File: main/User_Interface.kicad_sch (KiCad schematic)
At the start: 0 parts

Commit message: added UI, +12/gnd to 4 pin adapter symbol, added NMEA2000 gateway symbol
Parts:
- added UI: ~, symbol New_Library_0:Monitor
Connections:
- new net 4_pin_power: UI. (Radar_port_Ethernet)
- new net 9_pin_sonar: UI. (Radar_port_Ethernet)
- new net NMEA2000: UI. (Radar_port_Ethernet)
- new net Radar_port_ethernet: UI. (Radar_port_Ethernet)
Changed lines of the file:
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@@
 	(generator_version "8.0")
 	(paper "A4")
+	(hierarchical_label "Radar_port_ethernet"
+		(shape input)
+		(at 133.35 114.3 270)
+		(fields_autoplaced yes)
+		(effects
+			(font
+				(size 1.27 1.27)
+			)
+			(justify right)
+		)
+	)
+	(hierarchical_label "NMEA2000"
+		(shape input)
+		(at 138.43 114.3 270)
+		(fields_autoplaced yes)
+		(effects
+			(font
+				(size 1.27 1.27)
+			)
+			(justify right)
+		)
+	)
+	(hierarchical_label "4_pin_power"
+		(shape input)
+		(at 163.83 114.3 270)
+		(fields_autoplaced yes)
+		(effects
+			(font
+				(size 1.27 1.27)
+			)
+			(justify right)
+		)
+	)
+	(hierarchical_label "9_pin_sonar"
+		(shape input)
+		(at 168.91 114.3 270)
+		(fields_autoplaced yes)
+		(effects
+			(font
+				(size 1.27 1.27)
+			)
+			(justify right)
+		)
+	)
+	(symbol
+		(lib_id "New_Library_0:Monitor")
+		(at 151.13 99.06 0)
+		(unit 1)
+		(exclude_from_sim no)
+		(in_bom yes)
+		(on_board yes)
+		(dnp no)
+		(property "Reference" "UI"
+			(at 149.352 72.136 0)
+			(effects
+				(font
+					(size 1.27 1.27)
+				)
+				(justify left)
+			)
+		)
+		(property "Value" "~"
+			(at 177.8 93.98 0)
+			(effects
+				(font
+					(size 1.27 1.27)
+				)
+				(justify left)
+			)
+		)
+		(property "Footprint" ""
+			(at 151.13 99.06 0)
+			(effects
+				(font
+					(size 1.27 1.27)
+				)
+				(hide yes)
+			)
+		)
+		(property "Datasheet" ""
+			(at 151.13 99.06 0)
+			(effects
+				(font
+					(size 1.27 1.27)
+				)
+				(hide yes)
+			)
+		)
+		(property "Description" ""
+			(at 151.13 99.06 0)
+			(effects
+				(font
+					(size 1.27 1.27)
+				)
+				(hide yes)
+			)
+		)
+		(pin ""
+		)
+		(pin ""
+		)
+		(pin ""
+		)
+		(pin ""
+		)
+		(instances
+			(project ""
+				(path "/54fbbba9-a737-4199-9a4b-f9fa49b3de5e/3ec4e0ef-19c3-4e21-bb09-251ed42858ce"
+					(reference "UI")
+					(unit 1)
+				)
+			)
+		)
+	)
 )

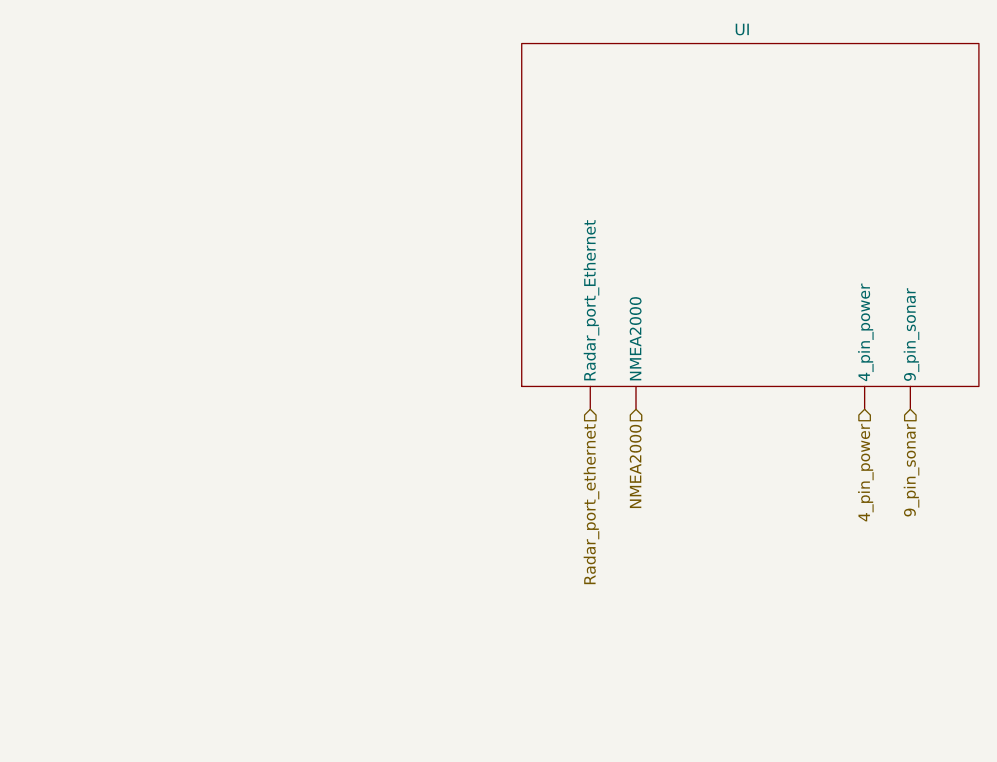
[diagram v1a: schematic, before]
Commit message: Added AMS, LEDs
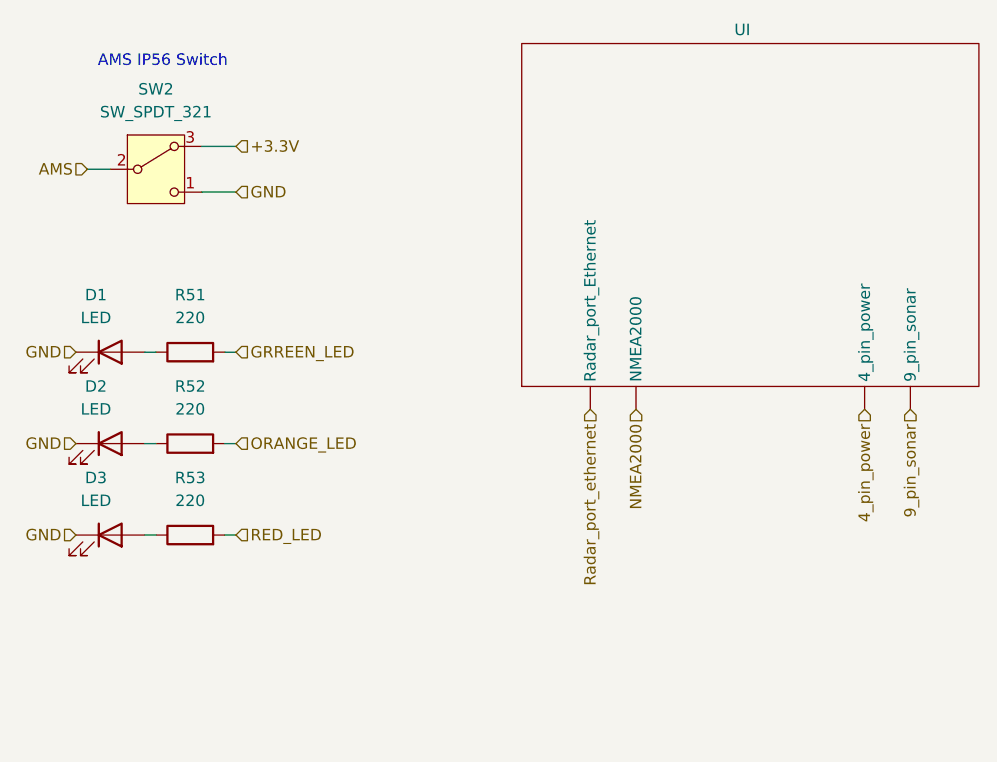
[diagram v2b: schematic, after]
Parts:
- added D1, D2, D3: LED, symbol Device:LED
- added R51, R52, R53: 220, symbol Device:R
- added SW2: SW_SPDT_321, symbol Switch:SW_SPDT_321
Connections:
- new net: D1.2 (A), R51.1
- new net: D3.2 (A), R53.1
- new net: D2.2 (A), R52.1
- new net +3.3V: SW2.3 (A)
- new net AMS: SW2.2 (B)
- new net GND: D1.1 (K), D2.1 (K), D3.1 (K), SW2.1 (C)
- new net GRREEN_LED: R51.2
- new net ORANGE_LED: R52.2
- new net RED_LED: R53.2
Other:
- note added: "AMS IP56 Switch"

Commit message: added logos, oranised sheets, final version
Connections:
- net Radar_port_ethernet renamed Radar
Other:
- company: (none) -> Designers: Krzysztof Grajek, Wojtek Kołodziej
- title: (none) -> UI schematic

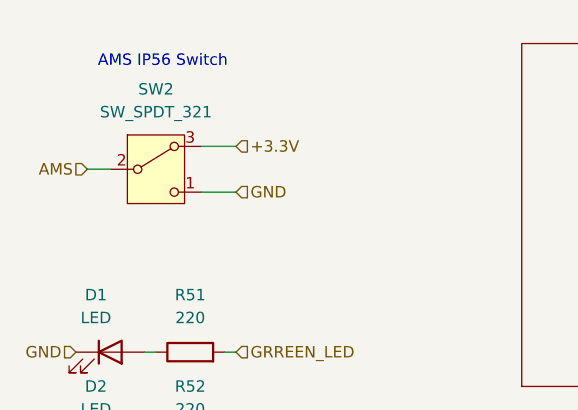
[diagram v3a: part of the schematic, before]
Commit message: removed AMS line, and previous switch ing UI. Renamed Switch in switching system to AMS
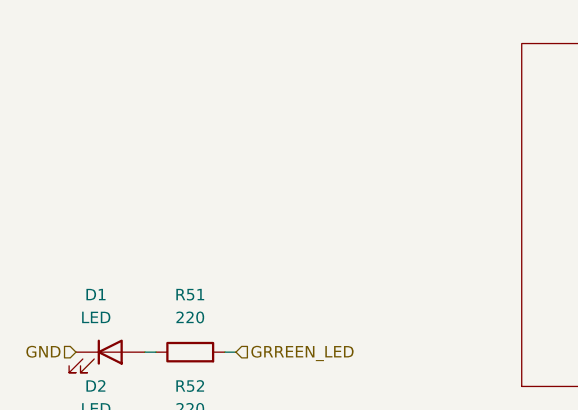
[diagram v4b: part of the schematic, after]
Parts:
- removed SW2: SW_SPDT_321, symbol Switch:SW_SPDT_321
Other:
- note removed: "AMS IP56 Switch"
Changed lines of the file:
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@@
 	(wire
 		(pts
-			(xy 77.47 87.63) (xy 80.01 87.63)
+			(xy 92.71 118.11) (xy 93.98 118.11)
 		)
 		(stroke
@@
 	(wire
 		(pts
-			(xy 92.71 118.11) (xy 93.98 118.11)
+			(xy 83.82 118.11) (xy 85.09 118.11)
 		)
 		(stroke
@@
 	(wire
 		(pts
-			(xy 83.82 118.11) (xy 85.09 118.11)
+			(xy 83.82 107.95) (xy 85.09 107.95)
 		)
 		(stroke
@@
 	(wire
 		(pts
-			(xy 90.17 85.09) (xy 93.98 85.09)
+			(xy 83.82 128.27) (xy 85.09 128.27)
 		)
 		(stroke
@@
 	(wire
 		(pts
-			(xy 83.82 107.95) (xy 85.09 107.95)
+			(xy 92.71 128.27) (xy 93.98 128.27)
 		)
 		(stroke
@@
 	(wire
 		(pts
-			(xy 83.82 128.27) (xy 85.09 128.27)
-		)
-		(stroke
-			(width 0)
-			(type default)
-		)
-	)
-	(wire
-		(pts
-			(xy 92.71 128.27) (xy 93.98 128.27)
-		)
-		(stroke
-			(width 0)
-			(type default)
-		)
-	)
-	(wire
-		(pts
 			(xy 92.71 107.95) (xy 93.98 107.95)
-		)
-		(stroke
-			(width 0)
-			(type default)
-		)
-	)
-	(wire
-		(pts
-			(xy 90.17 90.17) (xy 93.98 90.17)
 		)
 		(stroke
@@
 		)
 	)
-	(text "AMS IP56 Switch"
-		(exclude_from_sim no)
-		(at 85.852 75.692 0)
-		(effects
-			(font
-				(size 1.27 1.27)
-			)
-		)
-	)
 	(hierarchical_label "ORANGE_LED"
 		(shape input)
@@
 	(hierarchical_label "GND"
 		(shape input)
-		(at 93.98 90.17 0)
-		(fields_autoplaced yes)
-		(effects
-			(font
-				(size 1.27 1.27)
-			)
-			(justify left)
-		)
-	)
-	(hierarchical_label "GND"
-		(shape input)
 		(at 76.2 107.95 180)
-		(fields_autoplaced yes)
-		(effects
-			(font
-				(size 1.27 1.27)
-			)
-			(justify right)
-		)
-	)
-	(hierarchical_label "+3.3V"
-		(shape input)
-		(at 93.98 85.09 0)
-		(fields_autoplaced yes)
-		(effects
-			(font
-				(size 1.27 1.27)
-			)
-			(justify left)
-		)
-	)
-	(hierarchical_label "AMS"
-		(shape input)
-		(at 77.47 87.63 180)
 		(fields_autoplaced yes)
 		(effects
@@
 					(unit 1)
 				)
-			)
-		)
-	)
-	(symbol
-		(lib_id "Switch:SW_SPDT_321")
-		(at 85.09 87.63 0)
-		(unit 1)
-		(exclude_from_sim no)
-		(in_bom yes)
-		(on_board yes)
-		(dnp no)
-		(fields_autoplaced yes)
-		(property "Reference" "SW2"
-			(at 85.09 78.74 0)
-			(effects
-				(font
-					(size 1.27 1.27)
-				)
-			)
-		)
-		(property "Value" "SW_SPDT_321"
-			(at 85.09 81.28 0)
-			(effects
-				(font
-					(size 1.27 1.27)
-				)
-			)
-		)
-		(property "Footprint" ""
-			(at 85.09 97.79 0)
-			(effects
-				(font
-					(size 1.27 1.27)
-				)
-				(hide yes)
-			)
-		)
-		(property "Datasheet" "~"
-			(at 85.09 95.25 0)
-			(effects
-				(font
-					(size 1.27 1.27)
-				)
-				(hide yes)
-			)
-		)
-		(property "Description" "Switch, single pole double throw"
-			(at 85.09 87.63 0)
-			(effects
-				(font
-					(size 1.27 1.27)
-				)
-				(hide yes)
-			)
-		)
-		(pin "1"
-		)
-		(pin "3"
-		)
-		(pin "2"
-		)
-		(instances
-			(project ""
-				(path "/54fbbba9-a737-4199-9a4b-f9fa49b3de5e/3ec4e0ef-19c3-4e21-bb09-251ed42858ce"
-					(reference "SW2")
-					(unit 1)
-				)

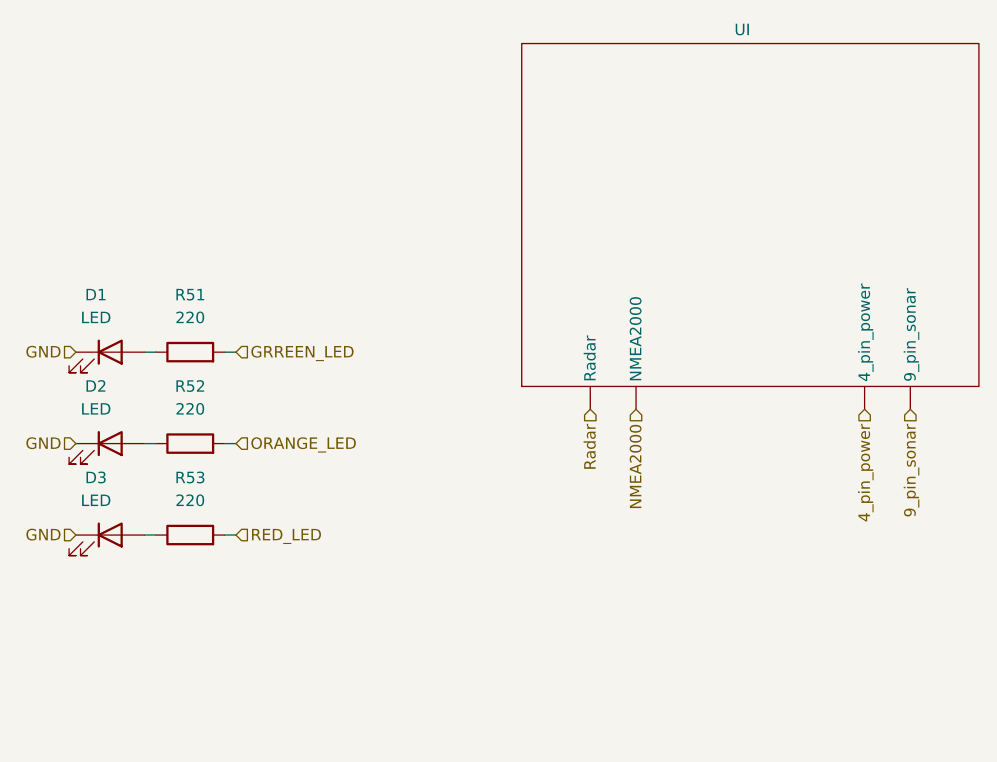
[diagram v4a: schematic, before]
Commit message: Updated digital gateway position. Removed NMEA lines
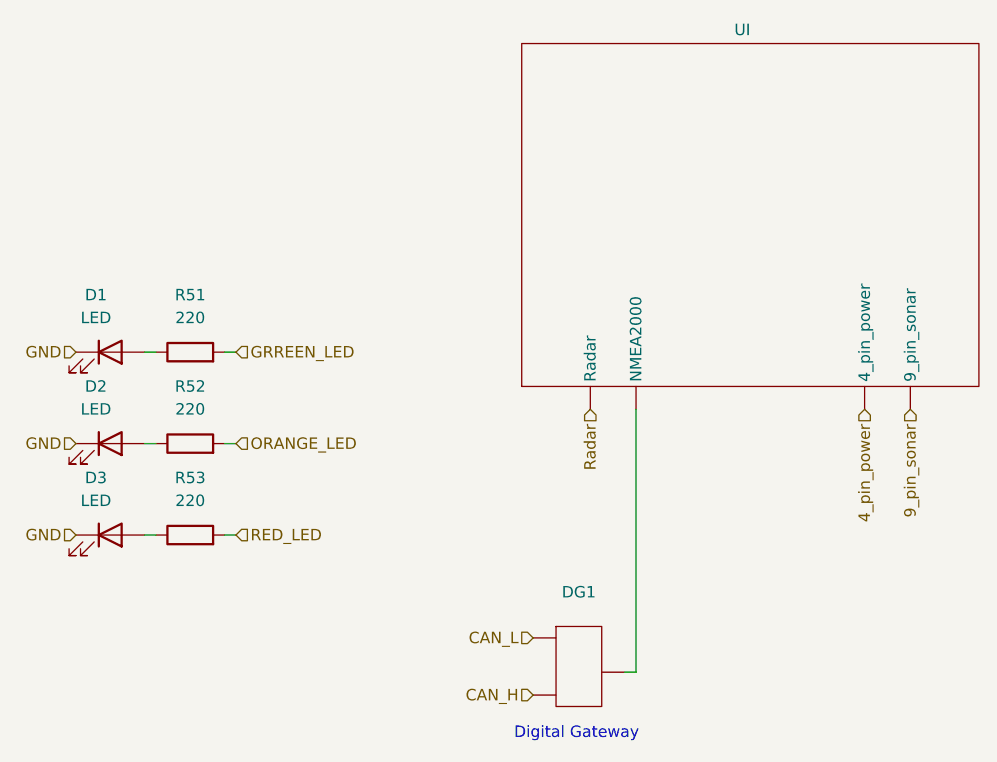
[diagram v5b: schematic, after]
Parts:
- added DG1: ~, symbol New_Library_0:DigitalGateway
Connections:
- net NMEA2000 is gone; now on net Radar: UI. (Radar)
- new net: DG1., UI. (Radar)
- new net CAN_H: DG1.
- new net CAN_L: DG1.
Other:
- note added: "Digital Gateway"
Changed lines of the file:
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@@
+	(wire
+		(pts
+			(xy 138.43 114.3) (xy 138.43 143.51)
+		)
+		(stroke
+			(width 0)
+			(type default)
+		)
+	)
 	(wire
 		(pts
@@
 		(pts
 			(xy 83.82 107.95) (xy 85.09 107.95)
+		)
+		(stroke
+			(width 0)
+			(type default)
+		)
+	)
+	(wire
+		(pts
+			(xy 137.16 143.51) (xy 138.43 143.51)
 		)
 		(stroke
@@
 		)
 	)
+	(text "Digital Gateway"
+		(exclude_from_sim no)
+		(at 131.826 150.368 0)
+		(effects
+			(font
+				(size 1.27 1.27)
+			)
+		)
+	)
+	(hierarchical_label "CAN_H"
+		(shape input)
+		(at 127 146.05 180)
+		(fields_autoplaced yes)
+		(effects
+			(font
+				(size 1.27 1.27)
+			)
+			(justify right)
+		)
+	)
 	(hierarchical_label "ORANGE_LED"
 		(shape input)
@@
 		)
 	)
-	(hierarchical_label "NMEA2000"
-		(shape input)
-		(at 138.43 114.3 270)
-		(fields_autoplaced yes)
-		(effects
-			(font
-				(size 1.27 1.27)
-			)
-			(justify right)
-		)
-	)
 	(hierarchical_label "4_pin_power"
 		(shape input)
@@
 		(shape input)
 		(at 76.2 128.27 180)
+		(fields_autoplaced yes)
+		(effects
+			(font
+				(size 1.27 1.27)
+			)
+			(justify right)
+		)
+	)
+	(hierarchical_label "CAN_L"
+		(shape input)
+		(at 127 139.7 180)
 		(fields_autoplaced yes)
 		(effects
@@
 					(unit 1)
 				)
+			)
+		)
+	)
+	(symbol
+		(lib_id "New_Library_0:DigitalGateway")
+		(at 132.08 143.51 0)
+		(unit 1)
+		(exclude_from_sim no)
+		(in_bom yes)
+		(on_board yes)
+		(dnp no)
+		(fields_autoplaced yes)
+		(property "Reference" "DG1"
+			(at 132.08 134.62 0)
+			(effects
+				(font
+					(size 1.27 1.27)
+				)
+			)
+		)
+		(property "Value" "~"
+			(at 132.08 137.16 0)
+			(effects
+				(font
+					(size 1.27 1.27)
+				)
+			)
+		)
+		(property "Footprint" ""
+			(at 132.08 143.51 0)
+			(effects
+				(font
+					(size 1.27 1.27)
+				)
+				(hide yes)
+			)
+		)
+		(property "Datasheet" ""
+			(at 132.08 143.51 0)
+			(effects
+				(font
+					(size 1.27 1.27)
+				)
+				(hide yes)
+			)
+		)
+		(property "Description" ""
+			(at 132.08 143.51 0)
+			(effects
+				(font
+					(size 1.27 1.27)
+				)
+				(hide yes)
+			)
+		)
+		(pin ""
+		)
+		(pin ""
+		)
+		(pin ""
+		)
+		(instances
+			(project ""
+				(path "/54fbbba9-a737-4199-9a4b-f9fa49b3de5e/3ec4e0ef-19c3-4e21-bb09-251ed42858ce"
+					(reference "DG1")
+					(unit 1)
+				)
